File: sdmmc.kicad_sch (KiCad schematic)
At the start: 12 parts, among them J1101 DM3AT-SF-PEJM5

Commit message: Add series termination, assign netclasses, fill schemas' descriptions
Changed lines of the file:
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@@
 		(rev "v0.0.1")
+	)
+	(text_box "micro-SD card interface provides the option to provide the operating system image on the SD card and to boot from it.\n\nThe supported micro-SD card size is up to 1 Terabyte.\n\nThe micro-SD card interface is human-interactable and thus has ESD TVS diodes for protection.\n\nThe micro-SD card interface is a push-push type and includes insertion detection capability. The insertion detection on the MPU side is active LOW.\nWhen the SD card is not inserted, the DET_A and DET_B pins are disconnected.\nWhen the SD card is connected, the DET_A and DET_B pins are connected."
+		(exclude_from_sim no)
+		(at 13.97 63.5 0)
+		(size 391.16 31.75)
+		(margins 0.9525 0.9525 0.9525 0.9525)
+		(stroke
+			(width -0.0001)
+			(type solid)
+		)
+		(fill
+			(type none)
+		)
+		(effects
+			(font
+				(size 2 2)
+			)
+			(justify left top)
+		)
 	)
 	(text_box "9. SDMMC"
@@
 		)
 	)
+	(text_box "micro-SD card interface"
+		(exclude_from_sim no)
+		(at 12.7 50.8 0)
+		(size 393.7 200.66)
+		(margins 0.9525 2 0.9525 0.9525)
+		(stroke
+			(width 0)
+			(type solid)
+		)
+		(fill
+			(type none)
+		)
+		(effects
+			(font
+				(size 5.08 5.08)
+				(thickness 1.016)
+				(bold yes)
+			)
+			(justify top)
+		)
+	)
+	(text_box "Notes"
+		(exclude_from_sim no)
+		(at 12.7 251.46 0)
+		(size 285.75 33.02)
+		(margins 0.9525 2 0.9525 0.9525)
+		(stroke
+			(width 0)
+			(type solid)
+		)
+		(fill
+			(type none)
+		)
+		(effects
+			(font
+				(size 5.08 5.08)
+				(thickness 1.016)
+				(bold yes)
+			)
+			(justify top)
+		)
+	)

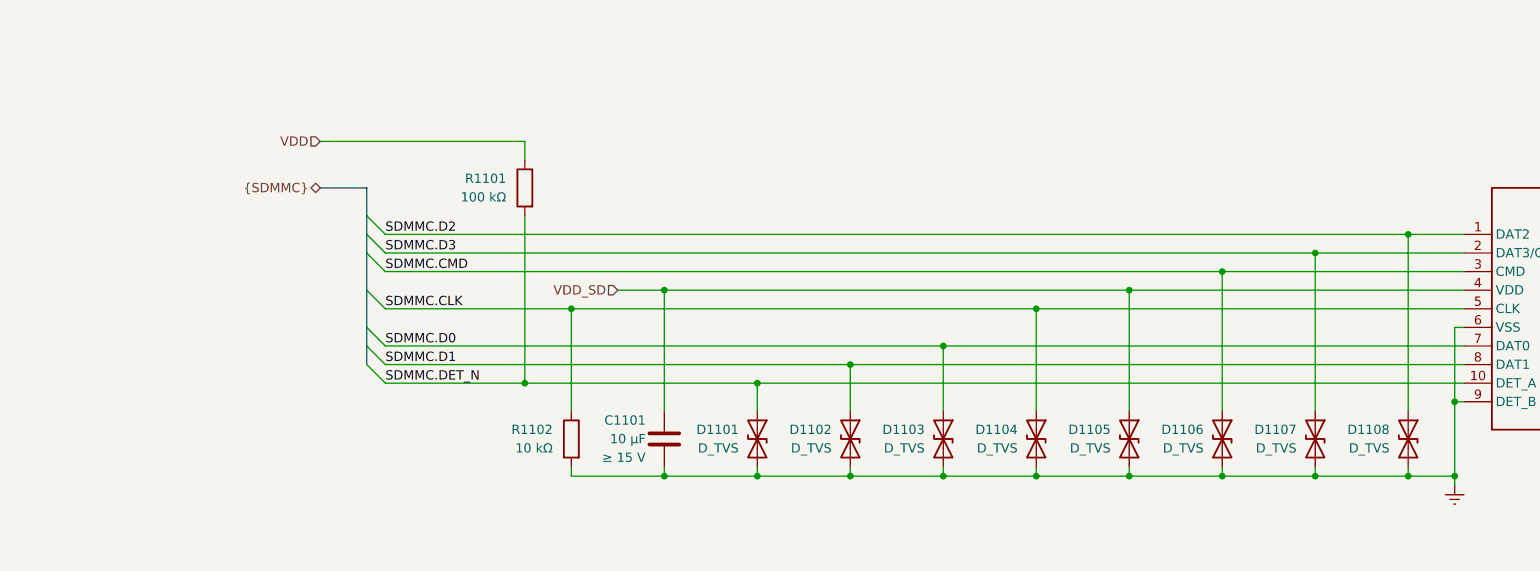
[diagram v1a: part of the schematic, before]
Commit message: Add series termination, refactor schematics
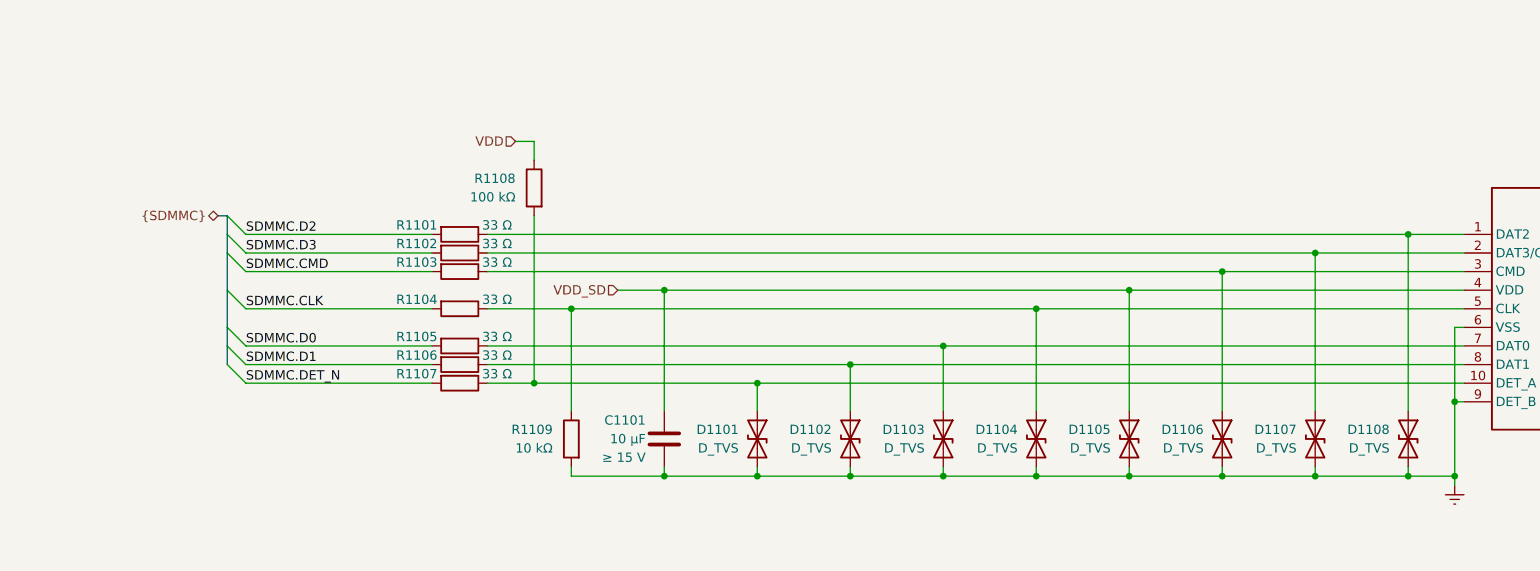
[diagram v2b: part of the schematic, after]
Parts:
- added R1101, R1102, R1103, R1104, R1105, R1106, R1107: 33 Ω, perfect_footprints:R_0402_1005Metric, symbol Device:R
- renumbered R1101 to R1108, R1102 to R1109
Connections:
- net SDMMC.CLK: now also R1104.2; no longer D1104.1 (A1), J1101.5 (CLK), R1109.1
- net SDMMC.CMD: now also R1103.2; no longer D1106.1 (A1), J1101.3 (CMD)
- net SDMMC.D0: now also R1105.2; no longer D1103.1 (A1), J1101.7 (DAT0)
- net SDMMC.D1: now also R1106.2; no longer D1102.1 (A1), J1101.8 (DAT1)
- net SDMMC.D2: now also R1101.2; no longer D1108.1 (A1), J1101.1 (DAT2)
- net SDMMC.D3: now also R1102.2; no longer D1107.1 (A1), J1101.2 (DAT3/CD)
- net SDMMC.DET_N: now also R1107.2; no longer D1101.1 (A1), J1101.10 (DET_A), R1108.2
- new net: D1102.1 (A1), J1101.8 (DAT1), R1106.1
- new net: D1108.1 (A1), J1101.1 (DAT2), R1101.1
- new net: D1103.1 (A1), J1101.7 (DAT0), R1105.1
- new net: D1107.1 (A1), J1101.2 (DAT3/CD), R1102.1
- new net: D1101.1 (A1), J1101.10 (DET_A), R1107.1, R1108.2
- new net: D1106.1 (A1), J1101.3 (CMD), R1103.1
- new net: D1104.1 (A1), J1101.5 (CLK), R1104.1, R1109.1
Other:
- moved on the sheet: R1108

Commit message: Refactor symbol properties
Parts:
- R1101, R1102, R1103, R1104, R1105, R1106, R1107, R1109: DigiKey Part Number 732-560112110020CT-ND -> (none)
- R1108: DigiKey Part Number 732-560112110019CT-ND -> (none)
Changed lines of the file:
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@@
-			)
-		)
-		(property "DigiKey Part Number" "732-560112110020CT-ND"
-			(at 118.11 144.78 0)
-			(effects
-				(font
-					(size 1.27 1.27)
-				)
-				(hide yes)
 			)
 		)
@@
 			)
 		)
-		(property "Temperature Coefficient" ""
-			(at 118.11 144.78 0)
-			(effects
-				(font
-					(size 1.27 1.27)
-				)
-				(hide yes)
-			)
-		)
 		(pin "2"
 		)
@@
 			)
 		)
-		(property "DigiKey Part Number" "732-560112110020CT-ND"
-			(at 118.11 129.54 0)
-			(effects
-				(font
-					(size 1.27 1.27)
-				)
-				(hide yes)
-			)
-		)
 		(property "MPN" "560112110020"
 			(at 118.11 129.54 0)
@@
 		)
 		(property "Manufacturer" "Würth Elektronik"
-			(at 118.11 129.54 0)
-			(effects
-				(font
-					(size 1.27 1.27)
-				)
-				(hide yes)
-			)
-		)
-		(property "Temperature Coefficient" ""
 			(at 118.11 129.54 0)
 			(effects
@@
 			)
 		)
-		(property "DigiKey Part Number" ""
-			(at 146.05 154.94 0)
-			(effects
-				(font
-					(size 1.27 1.27)
-				)
-				(hide yes)
-			)
-		)
 		(property "MPN" ""
 			(at 146.05 154.94 0)
@@
 				)
 				(justify left)
-			)
-		)
-		(property "Power" ""
-			(at 146.05 154.94 0)
-			(effects
-				(font
-					(size 1.27 1.27)
-				)
-				(hide yes)
-			)
-		)
-		(property "Temperature Coefficient" ""
-			(at 146.05 154.94 0)
-			(effects
-				(font
-					(size 1.27 1.27)
-				)
-				(hide yes)
 			)
 		)
@@
 			)
 		)
-		(property "DigiKey Part Number" "732-560112110020CT-ND"
-			(at 118.11 137.16 0)
-			(effects
-				(font
-					(size 1.27 1.27)
-				)
-				(hide yes)
-			)
-		)
 		(property "MPN" "560112110020"
 			(at 118.11 137.16 0)
@@
 		)
 		(property "Manufacturer" "Würth Elektronik"
-			(at 118.11 137.16 0)
-			(effects
-				(font
-					(size 1.27 1.27)
-				)
-				(hide yes)
-			)
-		)
-		(property "Temperature Coefficient" ""
 			(at 118.11 137.16 0)
 			(effects
@@
 			)
 		)
-		(property "DigiKey Part Number" "732-560112110020CT-ND"
-			(at 133.35 154.94 0)
-			(effects
-				(font
-					(size 1.27 1.27)
-				)
-				(hide yes)
-			)
-		)
 		(property "MPN" "560112110020"
 			(at 133.35 154.94 0)
@@
 			)
 		)
-		(property "Temperature Coefficient" ""
-			(at 133.35 154.94 0)
-			(effects
-				(font
-					(size 1.27 1.27)
-				)
-				(hide yes)
-			)
-		)
 		(pin "2"
 		)
@@
 			)
 		)
-		(property "DigiKey Part Number" "732-560112110020CT-ND"
-			(at 118.11 142.24 0)
-			(effects
-				(font
-					(size 1.27 1.27)
-				)
-				(hide yes)
-			)
-		)
 		(property "MPN" "560112110020"
 			(at 118.11 142.24 0)
@@
 		)
 		(property "Manufacturer" "Würth Elektronik"
-			(at 118.11 142.24 0)
-			(effects
-				(font
-					(size 1.27 1.27)
-				)
-				(hide yes)
-			)
-		)
-		(property "Temperature Coefficient" ""
 			(at 118.11 142.24 0)
 			(effects
@@
 			)
 		)
-		(property "DigiKey Part Number" "732-560112110019CT-ND"
-			(at 128.27 120.65 0)
-			(effects
-				(font
-					(size 1.27 1.27)
-				)
-				(hide yes)
-			)
-		)
 		(property "MPN" "560112110019"
 			(at 128.27 120.65 0)
@@
 			)
 		)
-		(property "Power" ""
-			(at 128.27 120.65 0)
-			(effects
-				(font
-					(size 1.27 1.27)
-				)
-				(hide yes)
-			)
-		)
-		(property "Temperature Coefficient" ""
-			(at 128.27 120.65 0)
-			(effects
-				(font
-					(size 1.27 1.27)
-				)
-				(hide yes)
-			)
-		)
 		(pin "2"
 		)
@@
 			)
 		)
-		(property "DigiKey Part Number" "732-560112110020CT-ND"
-			(at 118.11 147.32 0)
-			(effects
-				(font
-					(size 1.27 1.27)
-				)
-				(hide yes)
-			)
-		)
 		(property "MPN" "560112110020"
 			(at 118.11 147.32 0)
@@
 		)
 		(property "Manufacturer" "Würth Elektronik"
-			(at 118.11 147.32 0)
-			(effects
-				(font
-					(size 1.27 1.27)
-				)
-				(hide yes)
-			)
-		)
-		(property "Temperature Coefficient" ""
 			(at 118.11 147.32 0)
 			(effects
@@
 			)
 		)
-		(property "DigiKey Part Number" "732-560112110020CT-ND"
-			(at 118.11 127 0)
-			(effects
-				(font
-					(size 1.27 1.27)
-				)
-				(hide yes)
-			)
-		)
 		(property "MPN" "560112110020"
 			(at 118.11 127 0)
@@
 			)
 		)
-		(property "Temperature Coefficient" ""
-			(at 118.11 127 0)
-			(effects
-				(font
-					(size 1.27 1.27)
-				)
-				(hide yes)
-			)
-		)
 		(pin "2"
 		)
@@
 			)
 		)
-		(property "DigiKey Part Number" "732-560112110020CT-ND"
-			(at 118.11 132.08 0)
-			(effects
-				(font
-					(size 1.27 1.27)
-				)
-				(hide yes)
-			)
-		)
 		(property "MPN" "560112110020"
 			(at 118.11 132.08 0)
@@
 			(at 118.11 132.08 0)
 			(effects
-				(font
-					(size 1.27 1.27)
-				)
-				(hide yes)
-			)
-		)
-		(property "Temperature Coefficient" ""
-			(at 118.11 132.08 0)
-			(effects

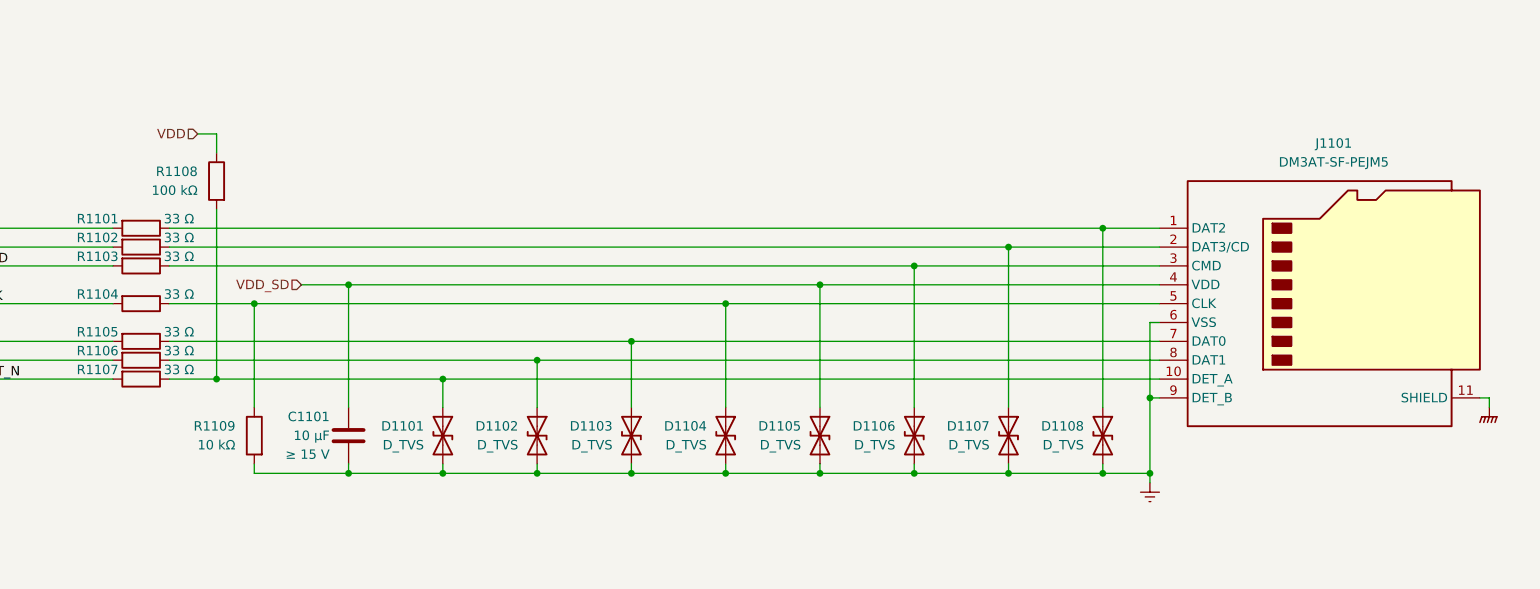
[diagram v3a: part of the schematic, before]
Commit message: Refactor SDMMC, UI, Wirelessg
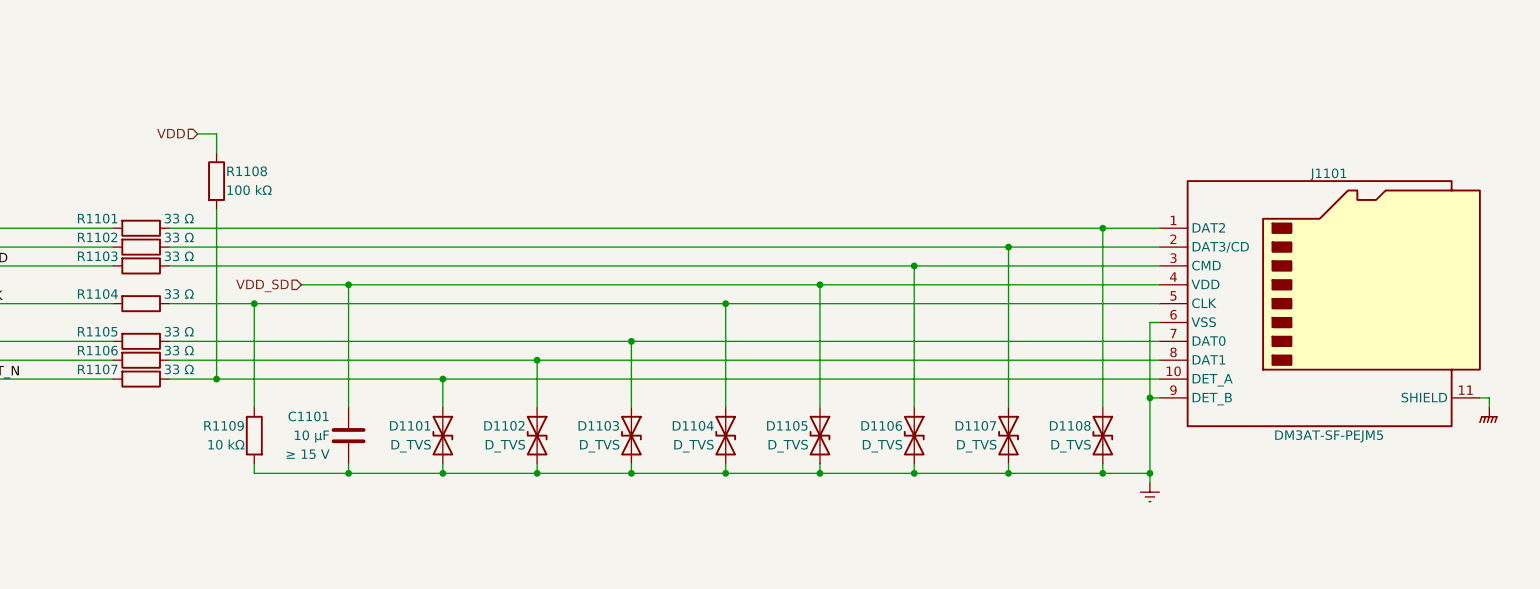
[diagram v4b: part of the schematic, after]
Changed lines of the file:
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@@
 		(dnp no)
 		(property "Reference" "D1108"
-			(at 245.11 153.6699 90)
+			(at 246.126 153.67 90)
 			(effects
 				(font
@@
 		)
 		(property "Value" "D_TVS"
-			(at 245.11 156.2099 90)
+			(at 246.126 156.21 90)
 			(effects
 				(font
@@
 		(dnp no)
 		(property "Reference" "D1103"
-			(at 181.61 153.6699 90)
+			(at 182.626 153.67 90)
 			(effects
 				(font
@@
 		)
 		(property "Value" "D_TVS"
-			(at 181.61 156.2099 90)
+			(at 182.626 156.21 90)
 			(effects
 				(font
@@
 		(on_board yes)
 		(dnp no)
-		(fields_autoplaced yes)
 		(property "Reference" "J1101"
-			(at 278.765 115.57 0)
-			(effects
-				(font
-					(size 1.27 1.27)
-				)
+			(at 278.13 120.396 0)
+			(effects
+				(font
+					(size 1.27 1.27)
+				)
+				(justify bottom)
 			)
 		)
 		(property "Value" "DM3AT-SF-PEJM5"
-			(at 278.765 118.11 0)
-			(effects
-				(font
-					(size 1.27 1.27)
-				)
+			(at 278.13 154.178 0)
+			(effects
+				(font
+					(size 1.27 1.27)
+				)
+				(justify top)
 			)
 		)
@@
 		(dnp no)
 		(property "Reference" "D1104"
-			(at 194.31 153.6699 90)
+			(at 195.326 153.67 90)
 			(effects
 				(font
@@
 		)
 		(property "Value" "D_TVS"
-			(at 194.31 156.2099 90)
+			(at 195.326 156.21 90)
 			(effects
 				(font
@@
 		(dnp no)
 		(property "Reference" "D1105"
-			(at 207.01 153.6699 90)
+			(at 208.026 153.67 90)
 			(effects
 				(font
@@
 		)
 		(property "Value" "D_TVS"
-			(at 207.01 156.2099 90)
+			(at 208.026 156.21 90)
 			(effects
 				(font
@@
 		(dnp no)
 		(property "Reference" "D1101"
-			(at 156.21 153.6699 90)
+			(at 157.226 153.67 90)
 			(effects
 				(font
@@
 		)
 		(property "Value" "D_TVS"
-			(at 156.21 156.2099 90)
+			(at 157.226 156.21 90)
 			(effects
 				(font
@@
 		(dnp no)
 		(property "Reference" "R1109"
-			(at 130.81 153.6699 0)
+			(at 132.08 153.67 0)
 			(effects
 				(font
@@
 		)
 		(property "Value" "10 kΩ"
-			(at 130.81 156.2099 0)
+			(at 132.08 156.21 0)
 			(effects
 				(font
@@
 		(lib_id "Device:R")
 		(at 128.27 120.65 0)
-		(mirror y)
 		(unit 1)
 		(exclude_from_sim no)
@@
 		(dnp no)
 		(property "Reference" "R1108"
-			(at 125.73 119.3799 0)
+			(at 129.54 119.38 0)
 			(effects
 				(font
@@
 		)
 		(property "Value" "100 kΩ"
-			(at 125.73 121.9199 0)
+			(at 129.54 121.92 0)
 			(effects
 				(font
@@
 		)
 		(property "Footprint" "perfect_footprints:R_0402_1005Metric"
-			(at 130.048 120.65 90)
+			(at 126.492 120.65 90)
 			(effects
 				(font
@@
 		(dnp no)
 		(property "Reference" "D1102"
-			(at 168.91 153.6699 90)
+			(at 169.926 153.67 90)
 			(effects
 				(font
@@
 		)
 		(property "Value" "D_TVS"
-			(at 168.91 156.2099 90)
+			(at 169.926 156.21 90)
 			(effects
 				(font
@@
 		(dnp no)
 		(property "Reference" "D1106"
-			(at 219.71 153.6699 90)
+			(at 220.726 153.67 90)
 			(effects
 				(font
@@
 		)
 		(property "Value" "D_TVS"
-			(at 219.71 156.2099 90)
+			(at 220.726 156.21 90)
 			(effects
 				(font
@@
 		(dnp no)
 		(property "Reference" "D1107"
-			(at 232.41 153.6699 90)
+			(at 233.426 153.67 90)
 			(effects
 				(font
@@
 		)
 		(property "Value" "D_TVS"
-			(at 232.41 156.2099 90)
-			(effects
-				(font
+			(at 233.426 156.21 90)
+			(effects
+				(font

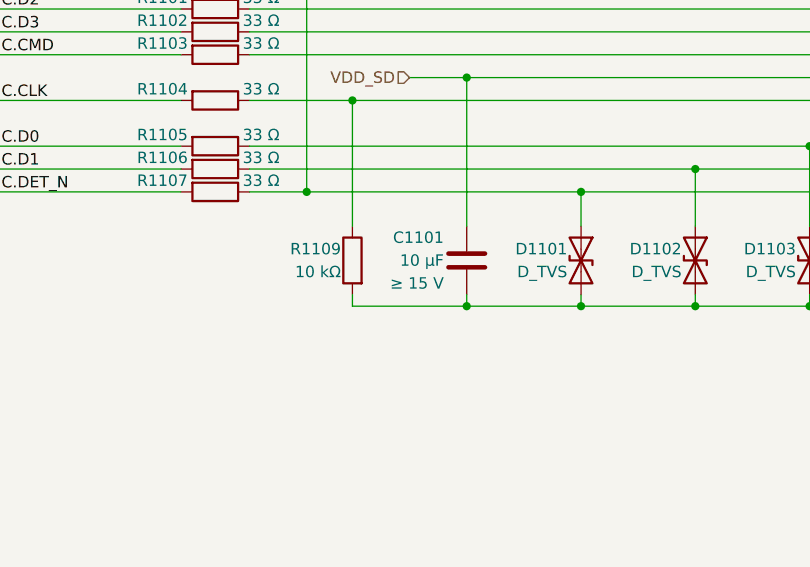
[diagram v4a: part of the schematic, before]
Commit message: Fix component values
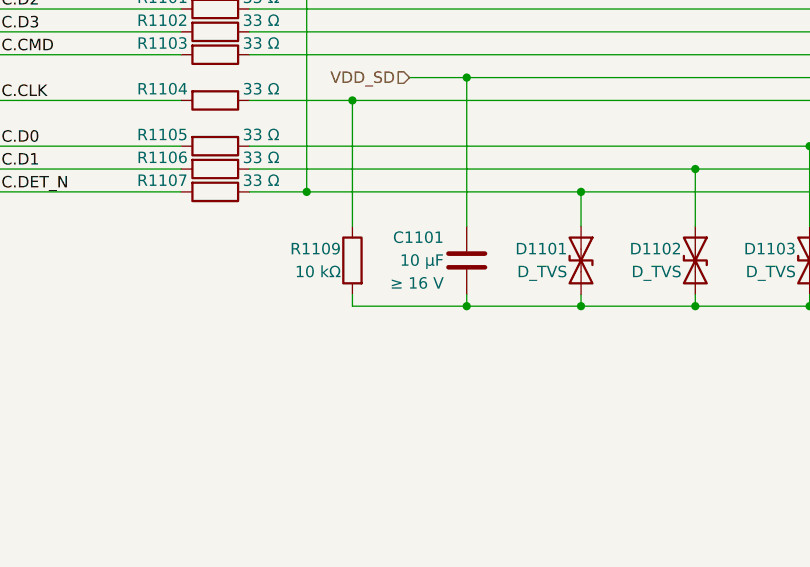
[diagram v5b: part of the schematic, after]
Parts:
- C1101: Voltage rating ≥ 15 V -> ≥ 16 V
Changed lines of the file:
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@@
 			)
 		)
-		(property "Voltage rating" "≥ 15 V"
+		(property "Voltage rating" "≥ 16 V"
 			(at 143.51 157.4801 0)
 			(effects

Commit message: Clean-up schematics
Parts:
- R1101, R1102, R1103, R1104, R1105, R1106, R1107: value 33 Ω -> 0 Ω
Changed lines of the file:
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@@
 			)
 		)
-		(property "Value" "33 Ω"
+		(property "Value" "0 Ω"
 			(at 121.158 144.272 90)
 			(effects
@@
 			)
 		)
-		(property "Value" "33 Ω"
+		(property "Value" "0 Ω"
 			(at 121.158 129.032 90)
 			(effects
@@
 			)
 		)
-		(property "Value" "33 Ω"
+		(property "Value" "0 Ω"
 			(at 121.158 136.652 90)
 			(effects
@@
 			)
 		)
-		(property "Value" "33 Ω"
+		(property "Value" "0 Ω"
 			(at 121.158 141.732 90)
 			(effects
@@
 			)
 		)
-		(property "Value" "33 Ω"
+		(property "Value" "0 Ω"
 			(at 121.158 146.812 90)
 			(effects
@@
 			)
 		)
-		(property "Value" "33 Ω"
+		(property "Value" "0 Ω"
 			(at 121.158 126.492 90)
 			(effects
@@
 			)
 		)
-		(property "Value" "33 Ω"
+		(property "Value" "0 Ω"
 			(at 121.158 131.572 90)
 			(effects
